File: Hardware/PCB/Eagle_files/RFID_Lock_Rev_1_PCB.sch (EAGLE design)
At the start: 38 parts, among them IC1 74AHCT125, J3 Servo, K1 351, T2 2N2222

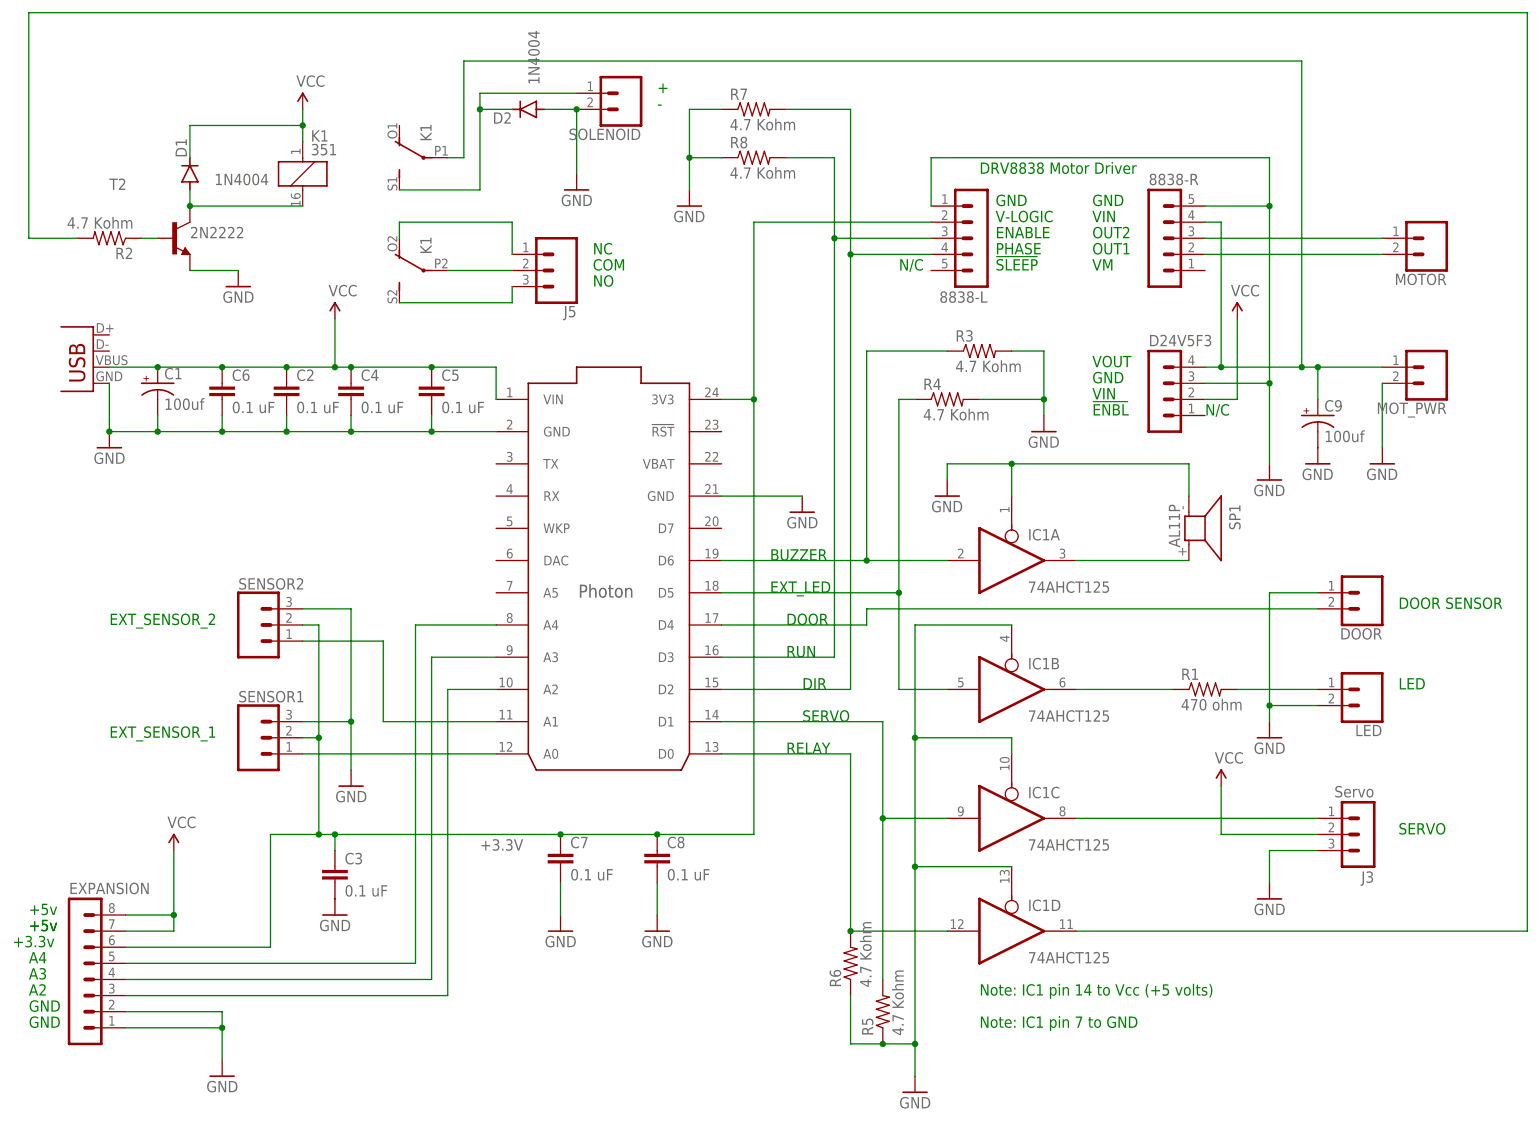
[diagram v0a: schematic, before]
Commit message: Updated PCB Files
Updated PCB files to Rev 1.  Also updated data sheets and misc information, but the parts list is NOT updated in this commit.
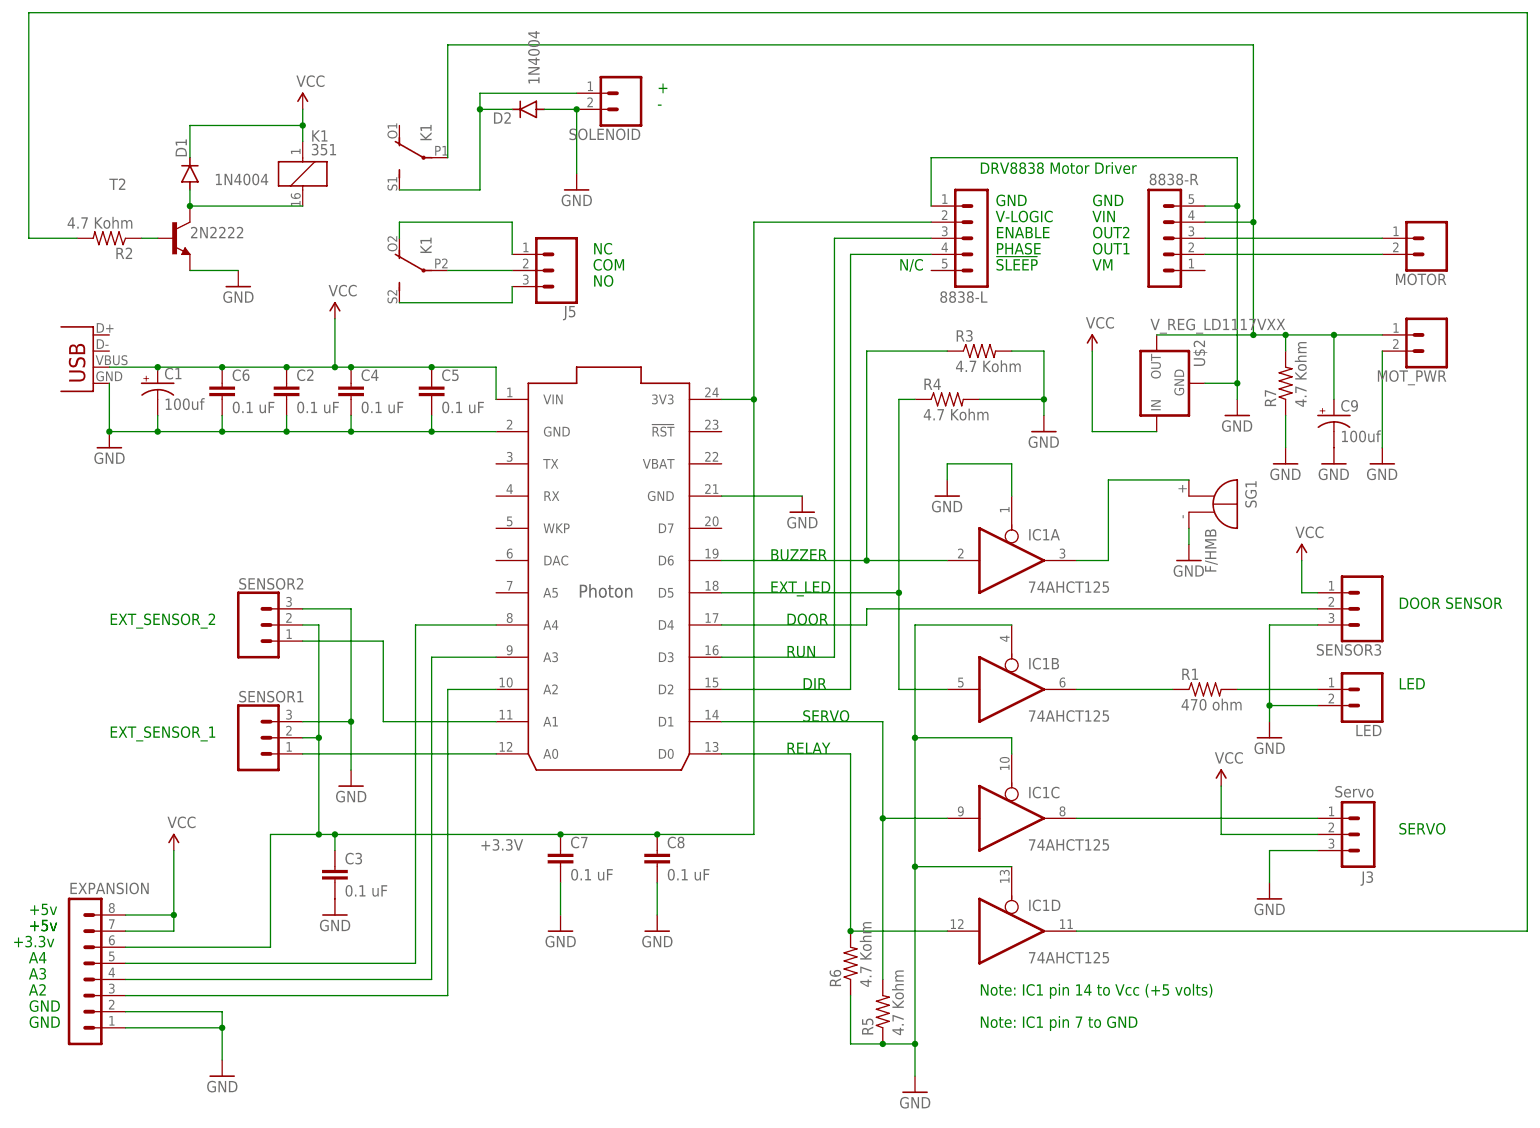
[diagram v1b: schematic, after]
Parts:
- removed D24V5F3: (no value), con-lstb:MA04-1
- removed DOOR: (no value), SparkFun-Connectors:CONN_023.5MM
- removed R8: 4.7 Kohm, rcl:R-US_0309/12
- removed SP1: AL11P, buzzer:AL11P
- added SENSOR3: (no value), SparkFun-Connectors:CONN_03SCREW
- added SG1: F/HMB, buzzer:F/HMB
- added U$2: V_REG_LD1117VXX, SparkFun-IC-Power:V_REG_LD1117VXX
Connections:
- removed net N$14: IC1A.O, SP1.2
- new net N$24: 8838-R.4, C9.+, K12.P, MOT_PWR.1, R7.2, U$2.OUT
- net GND: now also SENSOR3.3, SG1.-, U$2.GND; no longer D24V5F3.3, DOOR.1, R8.1, SP1.1
- net N$11: now also SENSOR3.2; no longer DOOR.2
- net N$12: no longer R7.2
- net N$5: no longer R8.2
- net N$6: now also IC1A.O, SG1.+; no longer 8838-R.4, C9.+, D24V5F3.4, K12.P, MOT_PWR.1
- net VCC: now also SENSOR3.1, U$2.IN; no longer D24V5F3.2
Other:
- note removed: "!ENBL"
- note removed: "VOUT"
- moved on the sheet: C9, MOT_PWR, R7
